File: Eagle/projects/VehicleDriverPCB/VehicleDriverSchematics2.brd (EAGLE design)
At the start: 100 x 80 mm, 8 parts, among them X1 1751248

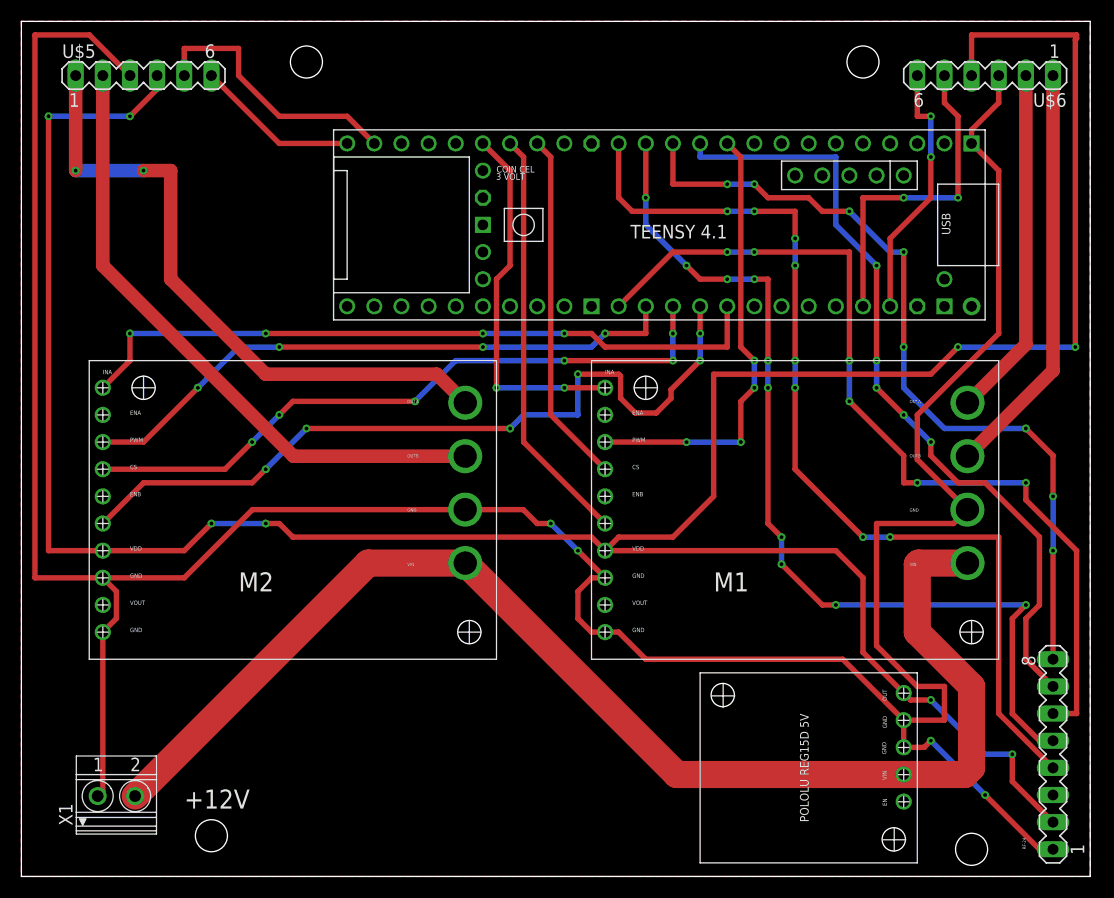
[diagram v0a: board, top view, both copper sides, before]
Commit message: Added new test project for improving in cmake, optimized PCB with new 12V terminal and silkscreen pin names
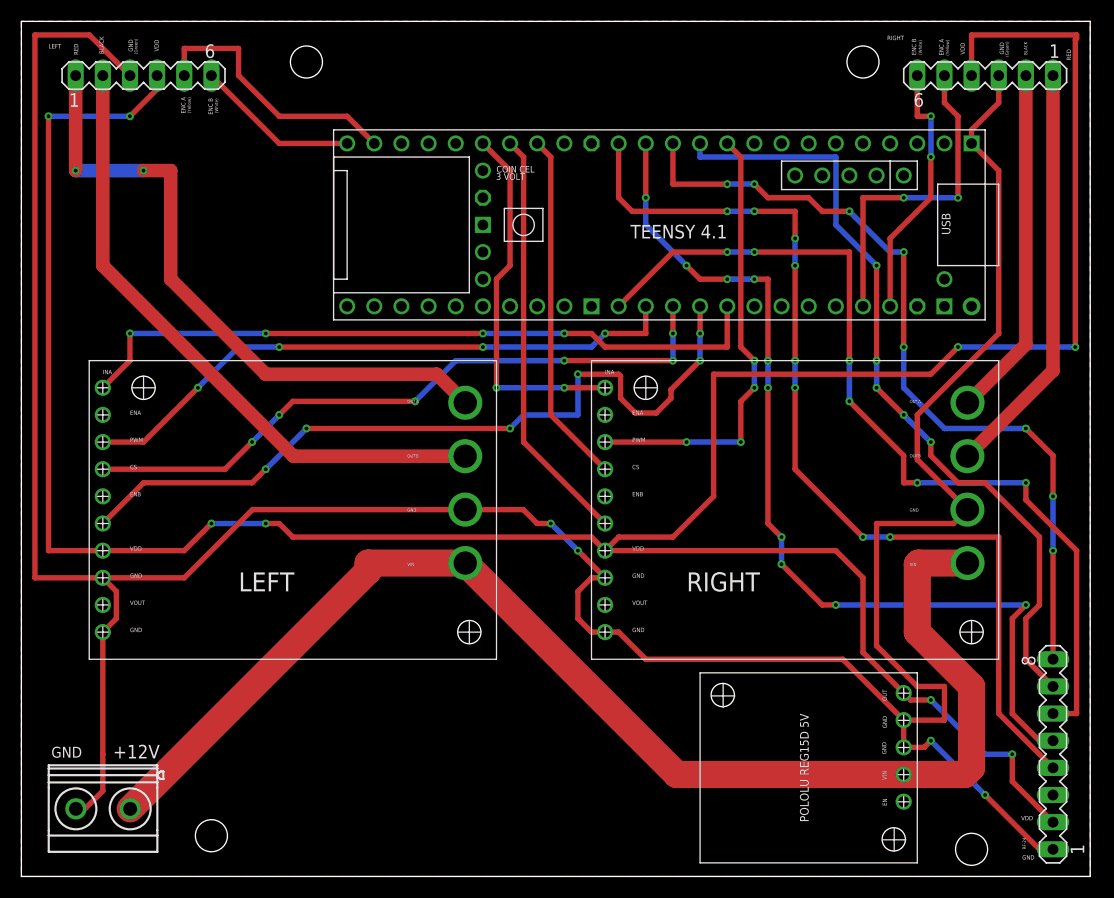
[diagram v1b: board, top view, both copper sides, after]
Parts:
- removed X1: 1751248, con-phoenix-350:1751248
- added X2: MKDSN1,5/2-5,08, con-phoenix-508:MKDSN1,5/2-5,08
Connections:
- net +12V: now also X2.1; no longer X1.2
- net GND: now also X2.2; no longer X1.1
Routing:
- net GND: track 285.7 -> 288.3 mm
- net +12V: track 121.6 -> 123.0 mm
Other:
- board text added: "(Green)"
- board text added: "(White)"
- board text added: "(Yellow)"
- board text added: "BLACK"
- board text added: "ENC A"
- board text added: "ENC B"
- board text added: "GND"
- board text added: "LEFT"
- board text added: "RED"
- board text added: "RIGHT"
- board text added: "VDD"
- board text removed: "M1"
- board text removed: "M2"
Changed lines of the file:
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@@
 <drawing>
 <settings>
-<setting alwaysvectorfont="yes"/>
+<setting alwaysvectorfont="no"/>
 <setting verticaltext="up"/>
 </settings>
-<grid distance="50" unitdist="mil" unit="mil" style="lines" multiple="1" display="no" altdistance="5" altunitdist="mil" altunit="mil"/>
+<grid distance="0.003125" unitdist="mic" unit="mm" style="lines" multiple="1" display="no" altdistance="5" altunitdist="mil" altunit="mil"/>
 <layers>
 <layer number="1" name="Top" color="4" fill="1" visible="yes" active="yes"/>
 <layer number="16" name="Bottom" color="1" fill="1" visible="yes" active="yes"/>
-<layer number="17" name="Pads" color="2" fill="1" visible="yes" active="yes"/>
+<layer number="17" name="Pads" color="2" fill="1" visible="no" active="yes"/>
 <layer number="18" name="Vias" color="2" fill="1" visible="yes" active="yes"/>
 <layer number="19" name="Unrouted" color="6" fill="1" visible="yes" active="yes"/>
@@
 <wire x1="100" y1="80" x2="0" y2="80" width="0" layer="20"/>
 <wire x1="0" y1="80" x2="0" y2="0" width="0" layer="20"/>
-<text x="20.32" y="26.67" size="1.778" layer="25">M2</text>
-<text x="64.77" y="26.67" size="1.778" layer="25">M1</text>
-<text x="15.24" y="6.35" size="1.778" layer="25">+12V</text>
+<text x="20.32" y="26.67" size="1.778" layer="25">LEFT</text>
+<text x="62.23" y="26.67" size="1.778" layer="25">RIGHT</text>
+<text x="8.566359375" y="11.038721875" size="1.27" layer="25">+12V</text>
 <hole x="26.67" y="76.2" drill="3"/>
 <hole x="78.74" y="76.2" drill="3"/>
 <hole x="17.78" y="3.81" drill="3"/>
 <hole x="88.9" y="2.54" drill="3"/>
+<text x="2.54" y="77.47" size="0.4064" layer="25">LEFT</text>
+<text x="10.022840625" y="78.311309375" size="0.4064" layer="25" rot="R270">GND</text>
+<text x="12.44283125" y="78.2941625" size="0.4064" layer="25" rot="R270">VDD</text>
+<text x="93.540875" y="5.25274375" size="0.4064" layer="25">VDD</text>
+<text x="93.63915625" y="1.578565625" size="0.4064" layer="25">GND</text>
+<text x="87.86431875" y="78.01125625" size="0.4064" layer="25" rot="R270">VDD</text>
+<text x="10.558940625" y="78.38104375" size="0.3048" layer="25" rot="R270">(Green)</text>
+<text x="91.529978125" y="78.05108125" size="0.4064" layer="25" rot="R270">GND</text>
+<text x="92.066078125" y="78.120815625" size="0.3048" layer="25" rot="R270">(Green)</text>
+<text x="2.8005625" y="11.113521875" size="1.016" layer="25">GND</text>
+<text x="81.001103125" y="78.248196875" size="0.4064" layer="25">RIGHT</text>
+<text x="14.941815625" y="72.925203125" size="0.4064" layer="25" rot="R270">ENC A</text>
+<text x="15.5462" y="72.90356875" size="0.3048" layer="25" rot="R270">(Yellow)</text>
+<text x="17.498425" y="72.816809375" size="0.4064" layer="25" rot="R270">ENC B</text>
+<text x="18.102809375" y="72.795175" size="0.3048" layer="25" rot="R270">(White)</text>
+<text x="85.873259375" y="78.358025" size="0.4064" layer="25" rot="R270">ENC A</text>
+<text x="86.487565625" y="78.286784375" size="0.3048" layer="25" rot="R270">(Yellow)</text>
+<text x="83.310725" y="78.388534375" size="0.4064" layer="25" rot="R270">ENC B</text>
+<text x="83.944871875" y="78.24784375" size="0.3048" layer="25" rot="R270">(White)</text>
+<text x="7.29655625" y="78.59125" size="0.4064" layer="25" rot="R270">BLACK</text>
+<text x="4.91555625" y="77.915778125" size="0.4064" layer="25" rot="R270">RED</text>
+<text x="93.80595625" y="78.0915625" size="0.3048" layer="25" rot="R270">BLACK</text>
+<text x="97.796678125" y="77.3976125" size="0.4064" layer="25" rot="R270">RED</text>
 </plain>
 <attributes>
@@
 <element name="U$3" library="VehicleDriverParts" package="POLOLU_MD15B" value="POLOLU_MD15B" x="53.34" y="20.32" smashed="yes"/>
 <element name="U$4" library="teensy" package="TENNSY41-E" value="TEENSY41-E" x="58.42" y="60.96" smashed="yes" rot="R180"/>
-<element name="U$5" library="VehicleDriverParts" package="MA06-1" value="MA06-1" x="11.43" y="74.93" smashed="yes">
-<attribute name="NAME" x="3.81" y="76.581" size="1.27" layer="25" ratio="10"/>
-<attribute name="VALUE" x="8.89" y="72.009" size="1.27" layer="27" ratio="10"/>
-</element>
-<element name="U$6" library="VehicleDriverParts" package="MA06-1" value="MA06-1" x="90.17" y="74.93" smashed="yes" rot="R180">
-<attribute name="NAME" x="97.79" y="73.279" size="1.27" layer="25" ratio="10" rot="R180"/>
-<attribute name="VALUE" x="92.71" y="77.851" size="1.27" layer="27" ratio="10" rot="R180"/>
-</element>
+<element name="U$5" library="VehicleDriverParts" package="MA06-1" value="MA06-1" x="11.43" y="74.93" smashed="yes"/>
+<element name="U$6" library="VehicleDriverParts" package="MA06-1" value="MA06-1" x="90.17" y="74.93" smashed="yes" rot="R180"/>
 <element name="U$7" library="VehicleDriverParts" package="MA08-1-RF24" value="MA08-1-RF24" x="96.52" y="11.43" smashed="yes" rot="R90"/>
 <element name="U$8" library="VehicleDriverParts" package="POLOLU_REG15D" value="POLOLU_REG15D" x="83.82" y="1.27" smashed="yes" rot="R90"/>
-<element name="X1" library="con-phoenix-350" library_urn="urn:adsk.eagle:library:174" package="1751248" package3d_urn="urn:adsk.eagle:package:9395/1" value="1751248" x="8.89" y="7.62" smashed="yes">
-<attribute name="MF" value="" x="27.94" y="-73.66" size="1.778" layer="27" display="off"/>
-<attribute name="MPN" value="" x="27.94" y="-73.66" size="1.778" layer="27" display="off"/>
-<attribute name="NAME" x="4.785" y="4.7625" size="1.27" layer="25" rot="R90"/>
-<attribute name="OC_FARNELL" value="unknown" x="27.94" y="-73.66" size="1.778" layer="27" display="off"/>
-<attribute name="OC_NEWARK" value="unknown" x="27.94" y="-73.66" size="1.778" layer="27" display="off"/>
-<attribute name="POPULARITY" value="24" x="27.94" y="-73.66" size="1.778" layer="27" display="off"/>
-<attribute name="VALUE" x="6.8375" y="11.7475" size="1.27" layer="27"/>
+<element name="X2" library="con-phoenix-508" library_urn="urn:adsk.eagle:library:176" package="MKDSN1,5/2-5,08" package3d_urn="urn:adsk.eagle:package:9630/1" value="MKDSN1,5/2-5,08" x="7.62" y="6.35" smashed="yes" rot="R180">
+<attribute name="POPULARITY" value="14" x="7.62" y="6.35" size="1.778" layer="27" rot="R180" display="off"/>
 </element>
 </elements>
@@
 <contactref element="U$6" pad="GND"/>
 <contactref element="U$7" pad="GND"/>
-<contactref element="X1" pad="1"/>
 <wire x1="10.16" y1="74.93" x2="6.36" y2="78.73" width="0.508" layer="1"/>
 <wire x1="6.36" y1="78.73" x2="1.27" y2="78.73" width="0.508" layer="1"/>
@@
 <wire x1="90.17" y1="7.62" x2="95.25" y2="2.54" width="0.508" layer="1"/>
 <wire x1="95.25" y1="2.54" x2="96.52" y2="2.54" width="0.508" layer="1"/>
-<wire x1="7.14" y1="7.52" x2="7.62" y2="8" width="0.508" layer="1"/>
-<wire x1="7.62" y1="8" x2="7.62" y2="22.86" width="0.508" layer="1"/>
+<wire x1="7.62" y1="22.86" x2="7.62" y2="11.43" width="0.508" layer="1"/>
+<wire x1="7.62" y1="11.43" x2="7.62" y2="8" width="0.508" layer="1"/>
 <wire x1="7.62" y1="27.94" x2="8.89" y2="26.67" width="0.508" layer="1"/>
 <wire x1="8.89" y1="26.67" x2="8.89" y2="24.13" width="0.508" layer="1"/>
@@
 <vertex x="100" y="80"/>
 </polygon>
+<contactref element="X2" pad="2"/>
+<wire x1="7.62" y1="8" x2="5.945" y2="6.325" width="0.508" layer="1"/>
+<wire x1="5.945" y1="6.325" x2="5.1011" y2="6.325" width="0.508" layer="1"/>
 </signal>
 <signal name="+5V">
@@
 <contactref element="U$2" pad="VIN"/>
 <contactref element="U$3" pad="VIN"/>
-<contactref element="X1" pad="2"/>
 <contactref element="U$8" pad="VIN"/>
-<wire x1="10.64" y1="7.52" x2="32.44" y2="29.32" width="2.54" layer="1"/>
 <wire x1="32.44" y1="29.32" x2="41.53" y2="29.32" width="2.54" layer="1"/>
 <wire x1="41.53" y1="29.32" x2="61.31" y2="9.54" width="2.54" layer="1"/>
@@
 <wire x1="83.82" y1="29.21" x2="83.93" y2="29.32" width="2.54" layer="1"/>
 <wire x1="83.93" y1="29.32" x2="88.52" y2="29.32" width="2.54" layer="1"/>
+<contactref element="X2" pad="1"/>
+<wire x1="10.1811" y1="6.325" x2="32.44" y2="28.5839" width="2.54" layer="1"/>
+<wire x1="32.44" y1="28.5839" x2="32.44" y2="29.32" width="2.54" layer="1"/>
 </signal>
 <signal name="N$1">
